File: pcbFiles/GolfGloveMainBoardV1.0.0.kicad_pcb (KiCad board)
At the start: 4 copper layers, 40 x 55.3 mm, 78 parts, among them J1 USB_C_Receptacle, J11 Conn_01x16_Male, J12 HOST_WAKE, J13 TP4, J14 Conn_01x02, J15 Conn_01x02, J16 Conn_01x02, J17 Conn_01x02, J2 Conn_01x06, J3 USB_C_Receptacle, J6 Screw_Terminal_01x02, J7 Conn_01x02, J8 Conn_01x02, J9 Conn_01x02, SW1 SW_SPDT, SW2 SW_Push, U1 MCP73831T-2ACI/OT, U2 XC6119N16A7R-G, U3 LSM9DS1TR, U4 CYW20719B1KUMLG, U5 LSM9DS1TR, U7 TPS63001DRCT, Y1 Crystal, Y2 Crystal_GND23

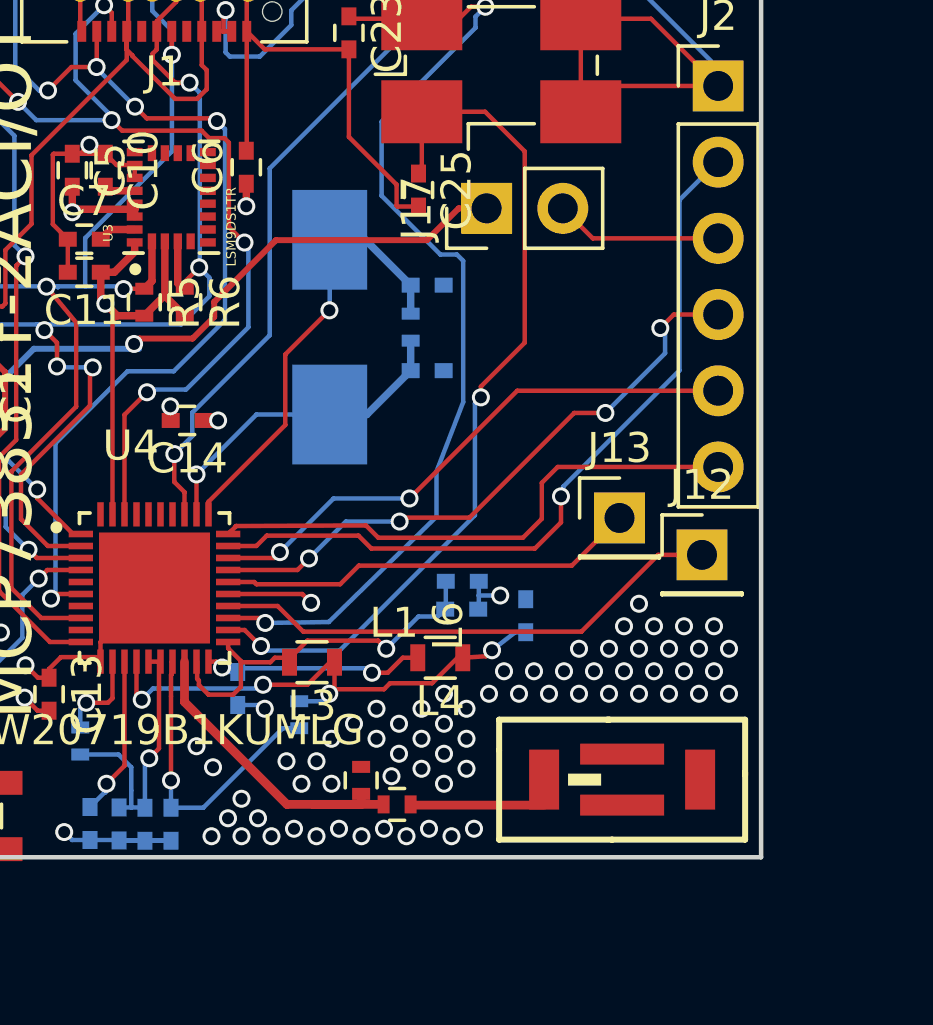
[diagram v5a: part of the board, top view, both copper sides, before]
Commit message: Fix Vias
Updated to brand new vias and also fixed plane issue around antenna
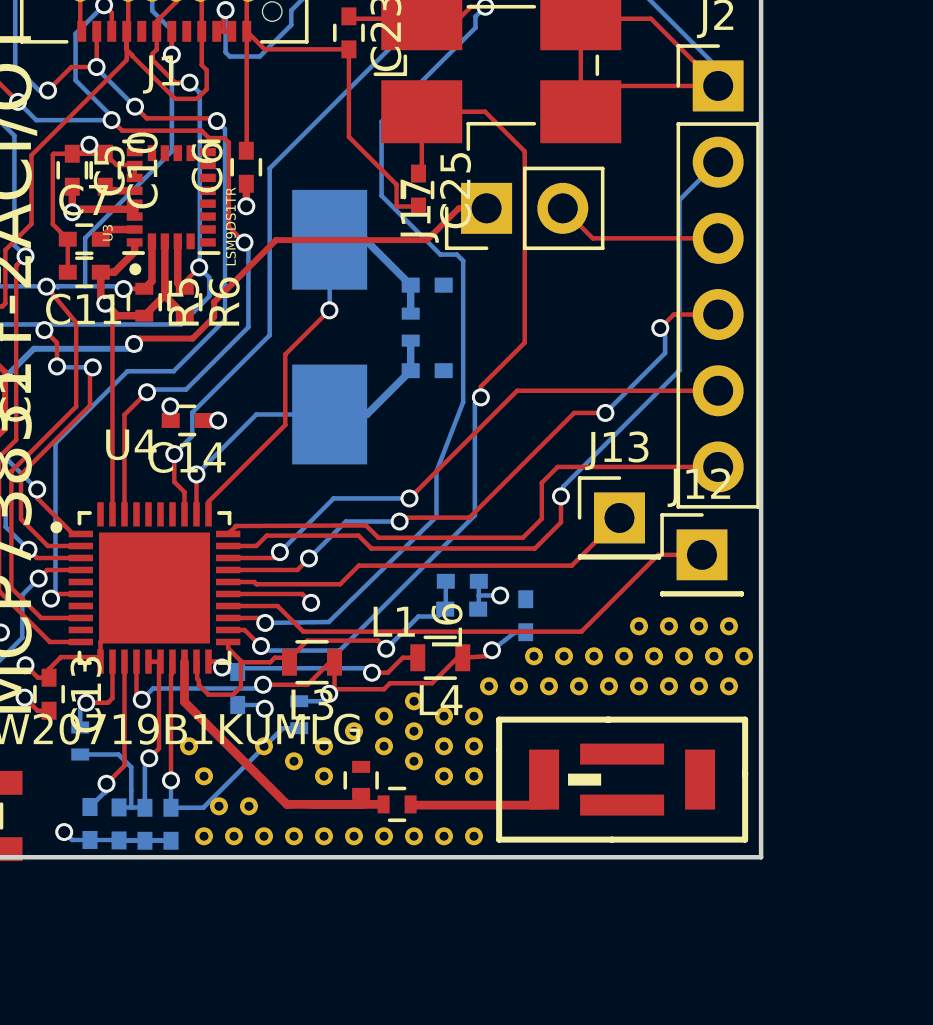
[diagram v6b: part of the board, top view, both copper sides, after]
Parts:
- added REF**: VIA-0.6mm, VIA-0.6mm, F.Cu at (126.0, 158.5)
- added REF**: VIA-0.6mm, VIA-0.6mm, F.Cu at (127.0, 159.0)
- added REF**: VIA-0.6mm, VIA-0.6mm, F.Cu at (128.0, 159.5)
- added REF**: VIA-0.6mm, VIA-0.6mm, F.Cu at (125.0, 161.5)
- added REF**: VIA-0.6mm, VIA-0.6mm, F.Cu at (131.0, 158.0)
- added REF**: VIA-0.6mm, VIA-0.6mm, F.Cu at (128.0, 158.5)
- added REF**: VIA-0.6mm, VIA-0.6mm, F.Cu at (131.0, 157.0)
- added REF**: VIA-0.6mm, VIA-0.6mm, F.Cu at (130.0, 158.5)
- added REF**: VIA-0.6mm, VIA-0.6mm, F.Cu at (139.5, 154.5)
- added REF**: VIA-0.6mm, VIA-0.6mm, F.Cu at (130.0, 157.5)
- added REF**: VIA-0.6mm, VIA-0.6mm, F.Cu at (131.0, 159.0)
- added REF**: VIA-0.6mm, VIA-0.6mm, F.Cu at (124.0, 161.5)
- added REF**: VIA-0.6mm, VIA-0.6mm, F.Cu at (131.0, 161.5)
- added REF**: VIA-0.6mm, VIA-0.6mm, F.Cu at (132.0, 161.5)
- added REF**: VIA-0.6mm, VIA-0.6mm, F.Cu at (132.0, 158.5)
- added REF**: VIA-0.6mm, VIA-0.6mm, F.Cu at (133.0, 158.5)
- added REF**: VIA-0.6mm, VIA-0.6mm, F.Cu at (133.0, 157.5)
- added REF**: VIA-0.6mm, VIA-0.6mm, F.Cu at (127.0, 161.5)
- added REF**: VIA-0.6mm, VIA-0.6mm, F.Cu at (133.0, 161.5)
- added REF**: VIA-0.6mm, VIA-0.6mm, F.Cu at (132.0, 159.5)
- added REF**: VIA-0.6mm, VIA-0.6mm, F.Cu at (132.0, 157.5)
- added REF**: VIA-0.6mm, VIA-0.6mm, F.Cu at (133.5, 156.5)
- added REF**: VIA-0.6mm, VIA-0.6mm, F.Cu at (124.0, 159.5)
- added REF**: VIA-0.6mm, VIA-0.6mm, F.Cu at (128.0, 161.5)
- added REF**: VIA-0.6mm, VIA-0.6mm, F.Cu at (130.0, 161.5)
- added REF**: VIA-0.6mm, VIA-0.6mm, F.Cu at (133.0, 159.5)
- added REF**: VIA-0.6mm, VIA-0.6mm, F.Cu at (140.0, 155.5)
- added REF**: VIA-0.6mm, VIA-0.6mm, F.Cu at (136.0, 155.5)
- added REF**: VIA-0.6mm, VIA-0.6mm, F.Cu at (126.0, 161.5)
- added REF**: VIA-0.6mm, VIA-0.6mm, F.Cu at (129.0, 161.5)
- added REF**: VIA-0.6mm, VIA-0.6mm, F.Cu at (135.0, 155.5)
- added REF**: VIA-0.6mm, VIA-0.6mm, F.Cu at (134.5, 156.5)
- added REF**: VIA-0.6mm, VIA-0.6mm, F.Cu at (138.0, 155.5)
- added REF**: VIA-0.6mm, VIA-0.6mm, F.Cu at (123.5, 158.5)
- added REF**: VIA-0.6mm, VIA-0.6mm, F.Cu at (129.0, 158.0)
- added REF**: VIA-0.6mm, VIA-0.6mm, F.Cu at (137.0, 155.5)
- added REF**: VIA-0.6mm, VIA-0.6mm, F.Cu at (142.0, 155.5)
- added REF**: VIA-0.6mm, VIA-0.6mm, F.Cu at (141.0, 155.5)
- added REF**: VIA-0.6mm, VIA-0.6mm, F.Cu at (141.5, 156.5)
- added REF**: VIA-0.6mm, VIA-0.6mm, F.Cu at (140.5, 156.5)
- added REF**: VIA-0.6mm, VIA-0.6mm, F.Cu at (139.5, 156.5)
- added REF**: VIA-0.6mm, VIA-0.6mm, F.Cu at (138.5, 156.5)
- added REF**: VIA-0.6mm, VIA-0.6mm, F.Cu at (137.5, 156.5)
- added REF**: VIA-0.6mm, VIA-0.6mm, F.Cu at (136.5, 156.5)
- added REF**: VIA-0.6mm, VIA-0.6mm, F.Cu at (124.5, 160.5)
- added REF**: VIA-0.6mm, VIA-0.6mm, F.Cu at (135.5, 156.5)
- added REF**: VIA-0.6mm, VIA-0.6mm, F.Cu at (139.0, 155.5)
- added REF**: VIA-0.6mm, VIA-0.6mm, F.Cu at (125.5, 160.5)
- added REF**: VIA-0.6mm, VIA-0.6mm, F.Cu at (140.5, 154.5)
- added REF**: VIA-0.6mm, VIA-0.6mm, F.Cu at (138.5, 154.5)
- added REF**: VIA-0.6mm, VIA-0.6mm, F.Cu at (141.5, 154.5)
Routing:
- net 3.3v: track 45.3 -> 218.0 mm
- net GND: vias 80 -> 14
- added copper zone on In2.Cu, net GND
- removed copper zone on In2.Cu, net 3.3v
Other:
- net class Default: via_dia 0.5 -> 0.45; via_drill 0.34 -> 0.2
- net class Small: via_dia 0.6 -> 0.45; via_drill 0.4 -> 0.2
- rule via_min_drill: 0.3 -> 0.2
- rule via_min_size: 0.4 -> 0.45

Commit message: Update Docs
@willcarroll7
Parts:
- removed the REF** at (126.0, 158.5)
- removed the REF** at (124.5, 160.5)
- added REF**: VIA-0.6mm, VIA-0.6mm, F.Cu at (148.3, 120.9)
- added REF**: VIA-0.6mm, VIA-0.6mm, F.Cu at (147.3, 128.3)
- added REF**: VIA-0.6mm, VIA-0.6mm, F.Cu at (146.9, 130.0)
- added REF**: VIA-0.6mm, VIA-0.6mm, F.Cu at (143.3, 121.4)
- added REF**: VIA-0.6mm, VIA-0.6mm, F.Cu at (146.3, 124.1)
- added REF**: VIA-0.6mm, VIA-0.6mm, F.Cu at (144.5, 128.7)
- added REF**: VIA-0.6mm, VIA-0.6mm, F.Cu at (109.7, 131.9)
- added REF**: VIA-0.6mm, VIA-0.6mm, F.Cu at (144.2, 147.9)
- added REF**: VIA-0.6mm, VIA-0.6mm, F.Cu at (127.2, 118.9)
- moved AE1 44.4 mm to (146.3, 116.0), turned to 90 degrees
- moved REF** 44.1 mm to (143.2, 112.4), turned to 90 degrees
- moved REF** 43.6 mm to (142.2, 111.9), turned to 90 degrees
- moved REF** 43.2 mm to (143.2, 113.4), turned to 90 degrees
- moved L1 42.7 mm to (147.2, 121.1), turned to 90 degrees
- moved REF** 42.6 mm to (142.2, 112.9), turned to 90 degrees
- moved REF** 42.5 mm to (148.2, 121.8), turned to 90 degrees
- moved REF** 42.2 mm to (143.2, 114.4), turned to 90 degrees
- moved REF** 42.1 mm to (141.2, 112.4), turned to 90 degrees
- moved REF** 41.9 mm to (148.0, 122.8), turned to 90 degrees
- moved REF** 41.6 mm to (142.2, 113.9), turned to 90 degrees
- moved REF** 41.4 mm to (148.0, 123.7), turned to 90 degrees
- moved REF** 41.3 mm to (143.2, 115.4), turned to 90 degrees
- moved REF** 41.1 mm to (141.2, 113.4), turned to 90 degrees
- moved REF** 40.8 mm to (146.2, 120.9), turned to 90 degrees
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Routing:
- net 3.3v: track 218.0 -> 330.0 mm
- net Net-(AE1-Pad1): track 4.35 -> 2.84 mm
- net Net-(L1-Pad1): track 11.3 -> 12.0 mm
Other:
- board size 40 x 55.3 mm -> 55.3 x 40 mm
- net class 3v added: clearance 0.2, trace_width 0.3, via_dia 0.45, via_drill 0.2
- board text added: "Golf Glove"
- board text added: "LEC"
- board text added: "REV1.0"

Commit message: Updates
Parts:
- removed L1, L6: L, Inductors_SMD:L_0402
- removed the REF** at (145.1, 128.0)
- removed Y2: Crystal_GND23, Crystals:Crystal_SMD_0603-4pin_6.0x3.5mm_HandSoldering
- added C19: C, Capacitors_SMD:C_0402, F.Cu at (147.2, 121.2)
- added C20: C, Capacitors_SMD:C_0402, F.Cu at (146.4, 123.0)
- added Y3: Crystal_GND24, Crystals:Crystal_SMD_0603-4pin_6.0x3.5mm_HandSoldering, F.Cu at (122.4, 120.0)
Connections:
- C22 pad 1: VBAT -> 3.3v
- U4 pad 13: VBAT -> 3.3v
- U4 pad 5: Net-(U4-Pad5) -> Net-(J11-Pad14)
- U4 pad 9: Net-(U4-Pad9) -> Net-(J11-Pad13)
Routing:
- net Net-(J11-Pad13): track 0.00 -> 17.4 mm, vias 0 -> 1
- net Net-(J11-Pad14): track 0.00 -> 16.2 mm, vias 0 -> 1
- net 3.3v: track 330.0 -> 338.7 mm, vias 11 -> 12
- net Net-(C23-Pad1): track 33.2 -> 38.7 mm
- net VBAT: track 5.34 -> 0.00 mm, vias 1 -> 0
- net Net-(J11-Pad16): track 13.4 -> 11.3 mm
- net GND: track 118.4 -> 116.6 mm
- net PSensor2: track 95.4 -> 96.9 mm
- net RST_N: track 21.5 -> 22.9 mm
- net Net-(C19-Pad1): track 12.0 -> 13.2 mm
- net BatteryOutChg: track 25.4 -> 24.2 mm
- net Sensor3: track 67.7 -> 68.7 mm
